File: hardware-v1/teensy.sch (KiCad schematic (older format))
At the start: 29 parts, among them J1 USB-MICRO-B-SHIELDED, P4 USB_POWER, P6 CORTEX_DEBUG, SW1 PROGRAM, U7 LP38691, U8 MK20DX256VLH7, U9 MKL02Z32VFG4, X1 CRYSTAL_SMD, Y2 32kHz

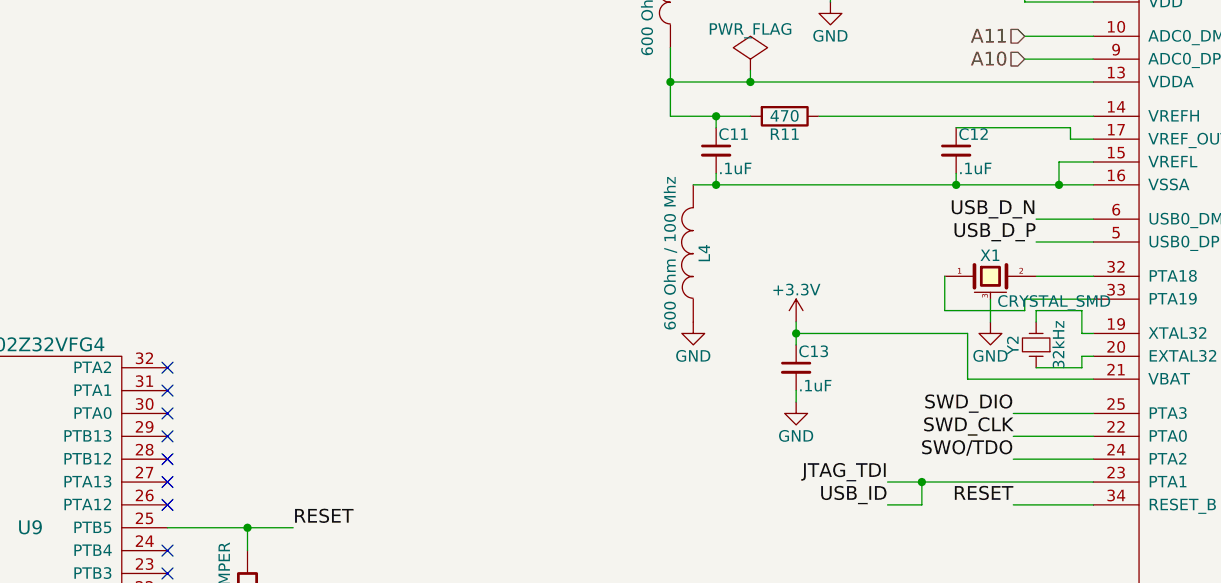
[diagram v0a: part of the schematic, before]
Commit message: Connect DEBUG line to MK02 reset line (with 0 ohm)
With a 0 ohm so that when PJRC comes up with bootloader that do not need
it, we will remove it.
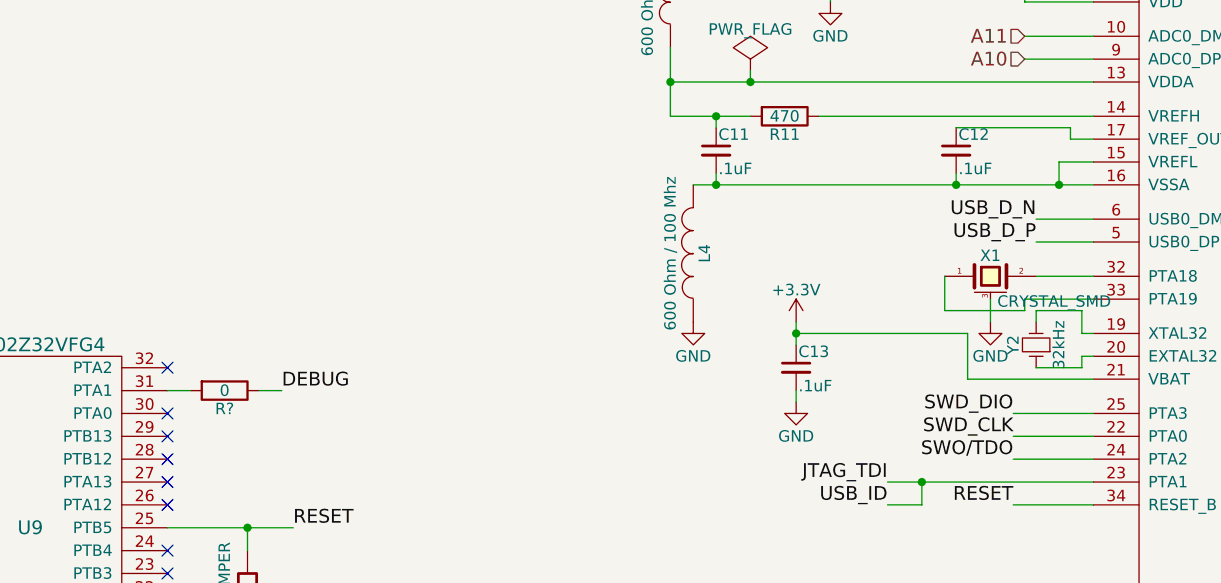
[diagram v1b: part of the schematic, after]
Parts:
- added R?: 0, symbol R
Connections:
- net DEBUG: now also R?.1
- net at U9.31 (PTA1): now also R?.2
- no-connect marks 21 -> 20
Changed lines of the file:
@@
 NoConn ~ 3000 3800
 NoConn ~ 3000 3700
-NoConn ~ 3000 3600
 NoConn ~ 3000 3500
 Text Label 1100 4200 2    60   ~ 0
@@
 	7050 2600 6900 2600
 Wire Wire Line
-	6900 2600 6900 2700
+	6900 2700 6900 2600
 Connection ~ 6900 2700
 Wire Wire Line
@@
 Wire Wire Line
 	4100 4900 4100 4950
+Wire Wire Line
+	3000 3600 3100 3600
+$Comp
+L R R?
+U 1 1 569DEDB1
+P 3250 3600
+F 0 "R?" V 3330 3600 50  0000 C CNN
+F 1 "0" V 3250 3600 50  0000 C CNN
+F 2 "" V 3180 3600 50  0000 C CNN
+F 3 "" H 3250 3600 50  0000 C CNN
+	1    3250 3600
+	0    1    1    0
+$EndComp
+Wire Wire Line
+	3400 3600 3500 3600
+Text Label 3500 3600 0    60   ~ 0
+DEBUG
 $EndSCHEMATC

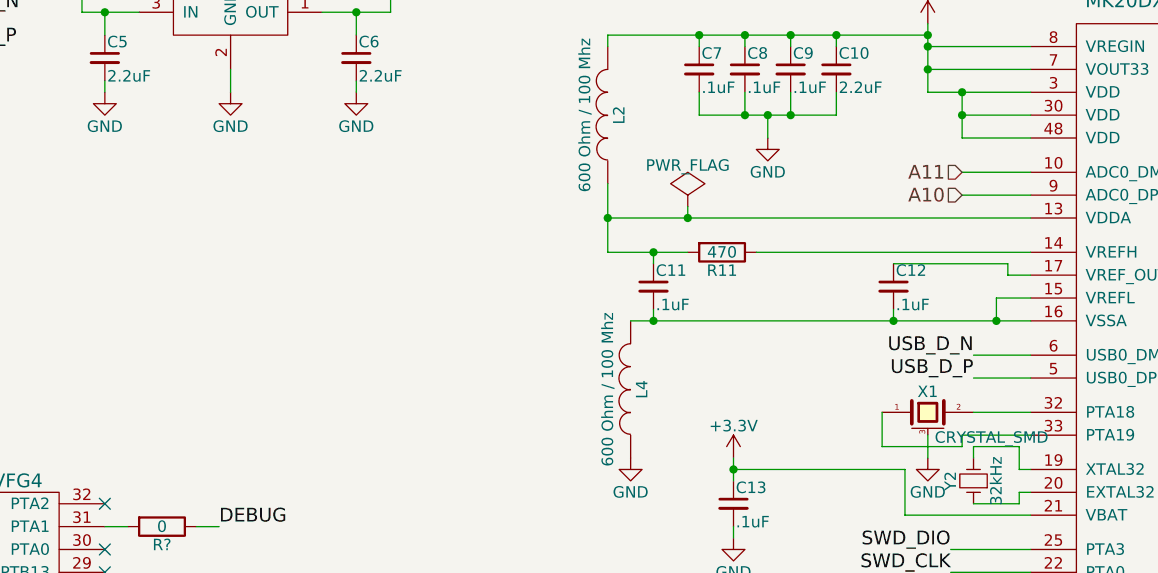
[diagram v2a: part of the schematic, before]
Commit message: Jumper to select Ser2 role + 3V voltage ref
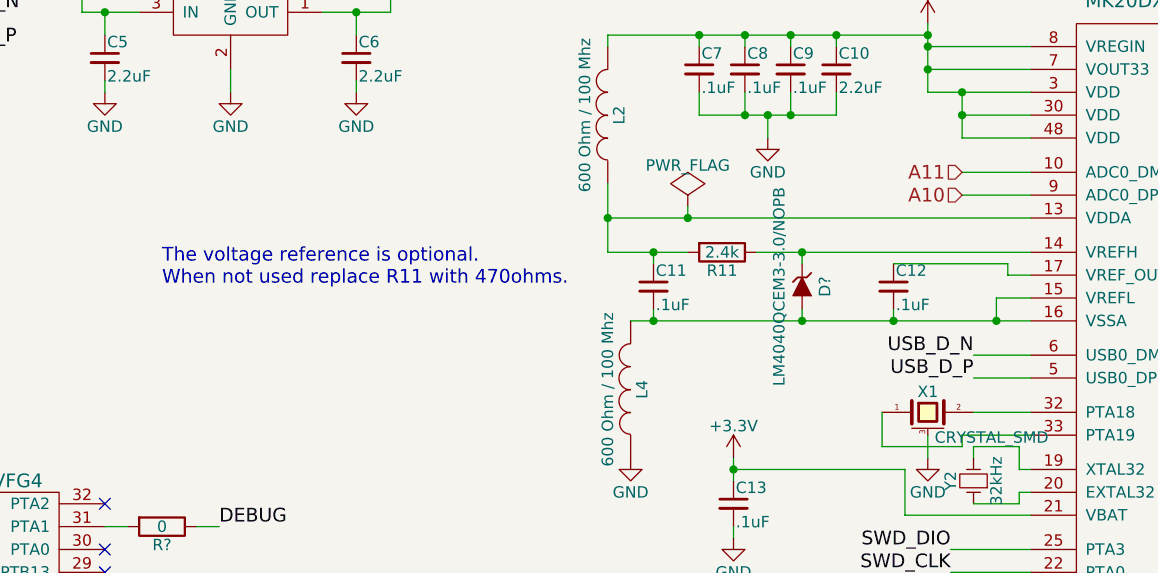
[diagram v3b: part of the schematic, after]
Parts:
- added D?: LM4040QCEM3-3.0/NOPB, symbol ZENERsmall
- R11: value 470 -> 2.4k
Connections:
- net at R11.1, U8.14 (VREFH): now also D?.1 (K)
- net at C11.2, C12.2, L4.2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: now also D?.2 (A)
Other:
- note added: "The voltage reference is optional.\nWhen not used replace R11 with 470ohms."
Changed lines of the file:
@@
 P 5700 2400
 F 0 "R11" V 5780 2400 50  0000 C CNN
-F 1 "470" V 5700 2400 50  0000 C CNN
+F 1 "2.4k" V 5700 2400 50  0000 C CNN
 F 2 "Resistors_SMD:R_0603_HandSoldering" V 5630 2400 30  0001 C CNN
 F 3 "" H 5700 2400 30  0000 C CNN
@@
 	7050 2600 6900 2600
 Wire Wire Line
-	6900 2700 6900 2600
+	6900 2600 6900 2700
 Connection ~ 6900 2700
 Wire Wire Line
@@
 Text Label 3500 3600 0    60   ~ 0
 DEBUG
+$Comp
+L ZENERsmall D?
+U 1 1 56ABEAB8
+P 6050 2550
+F 0 "D?" H 6050 2650 50  0000 C CNN
+F 1 "LM4040QCEM3-3.0/NOPB" H 6050 2450 50  0000 C CNN
+F 2 "" H 6050 2550 50  0000 C CNN
+F 3 "" H 6050 2550 50  0000 C CNN
+	1    6050 2550
+	0    1    1    0
+$EndComp
+Wire Wire Line
+	6050 2450 6050 2400
+Connection ~ 6050 2400
+Wire Wire Line
+	6050 2650 6050 2700
+Connection ~ 6050 2700
+Text Notes 3250 2550 0    60   ~ 0
+The voltage reference is optional.\nWhen not used replace R11 with 470ohms.
 $EndSCHEMATC

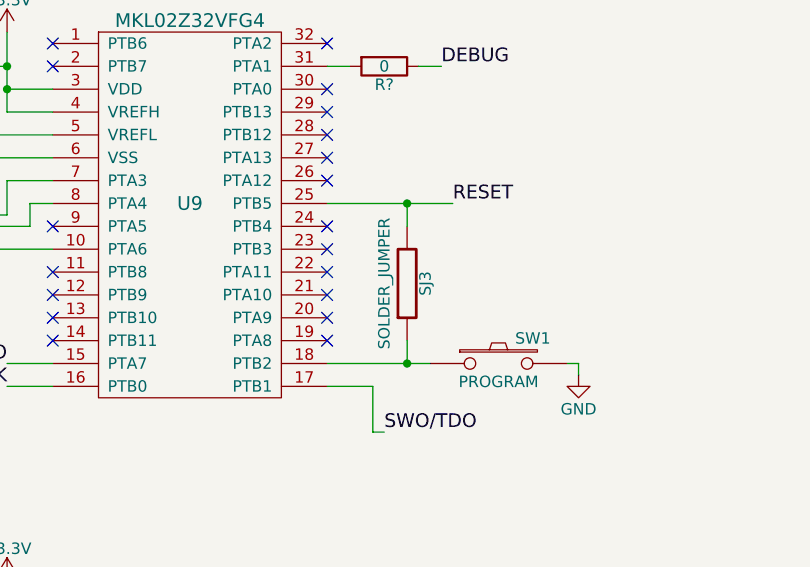
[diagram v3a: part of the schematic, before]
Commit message: Removed solder jumper on the reset line by a DNP 0 ohms
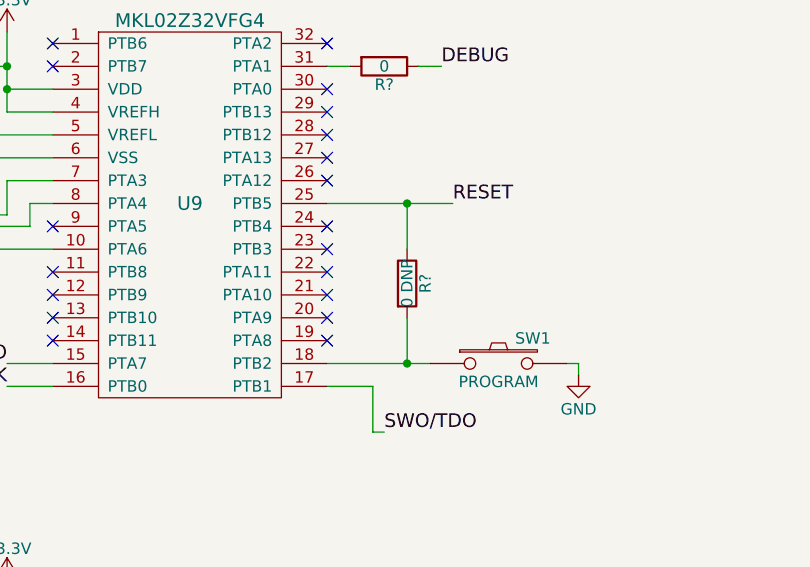
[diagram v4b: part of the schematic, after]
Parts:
- removed SJ3: SOLDER_JUMPER, bb:SolderJumper, symbol SOLDER_JUMPER
- added R?: 0 DNP, symbol R
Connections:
- net RESET: now also R?.1
- net at SW1.1, U9.18 (PTB2): now also R?.2
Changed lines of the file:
@@
 Wire Wire Line
 	1350 3600 1350 3650
-$Comp
-L SOLDER_JUMPER SJ3
-U 1 1 56652374
-P 3350 4550
-F 0 "SJ3" V 3430 4550 50  0000 C CNN
-F 1 "SOLDER_JUMPER" V 3250 4550 50  0000 C CNN
-F 2 "bb:SolderJumper" H 3350 4550 60  0001 C CNN
-F 3 "" H 3350 4550 60  0000 C CNN
-	1    3350 4550
-	1    0    0    1
-$EndComp
 Wire Wire Line
-	3350 4300 3350 4200
+	3350 4200 3350 4400
 Connection ~ 3350 4200
 Wire Wire Line
-	3350 4800 3350 4900
+	3350 4700 3350 4900
 Connection ~ 3350 4900
 Wire Wire Line
@@
 Text Notes 3250 2550 0    60   ~ 0
 The voltage reference is optional.\nWhen not used replace R11 with 470ohms.
+$Comp
+L R R?
+U 1 1 56AD8AD1
+P 3350 4550
+F 0 "R?" V 3430 4550 50  0000 C CNN
+F 1 "0 DNP" V 3350 4550 50  0000 C CNN
+F 2 "" V 3280 4550 50  0000 C CNN
+F 3 "" H 3350 4550 50  0000 C CNN
+	1    3350 4550
+	1    0    0    -1
+$EndComp
 $EndSCHEMATC

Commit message: re-annotate schematic
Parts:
- gave numbers to parts that had none: 3
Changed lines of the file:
@@
 $EndComp
 $Comp
-L GND #PWR033
+L GND #PWR44
 U 1 1 5658E841
 P 6850 5300
-F 0 "#PWR033" H 6850 5050 50  0001 C CNN
+F 0 "#PWR44" H 6850 5050 50  0001 C CNN
 F 1 "GND" H 6850 5150 50  0000 C CNN
 F 2 "" H 6850 5300 60  0000 C CNN
@@
 $EndComp
 $Comp
-L +3.3V #PWR034
+L +3.3V #PWR40
 U 1 1 5658ECFF
 P 1600 3450
-F 0 "#PWR034" H 1600 3300 50  0001 C CNN
+F 0 "#PWR40" H 1600 3300 50  0001 C CNN
 F 1 "+3.3V" H 1600 3590 50  0000 C CNN
 F 2 "" H 1600 3450 60  0000 C CNN
@@
 $EndComp
 $Comp
-L GND #PWR035
+L GND #PWR42
 U 1 1 5658ED8D
 P 1400 4050
-F 0 "#PWR035" H 1400 3800 50  0001 C CNN
+F 0 "#PWR42" H 1400 3800 50  0001 C CNN
 F 1 "GND" H 1400 3900 50  0000 C CNN
 F 2 "" H 1400 4050 60  0000 C CNN
@@
 $EndComp
 $Comp
-L GND #PWR036
+L GND #PWR43
 U 1 1 5658F088
 P 4100 4950
-F 0 "#PWR036" H 4100 4700 50  0001 C CNN
+F 0 "#PWR43" H 4100 4700 50  0001 C CNN
 F 1 "GND" H 4100 4800 50  0000 C CNN
 F 2 "" H 4100 4950 60  0000 C CNN
@@
 $EndComp
 $Comp
-L +3.3V #PWR037
+L +3.3V #PWR45
 U 1 1 56590BBB
 P 1600 5850
-F 0 "#PWR037" H 1600 5700 50  0001 C CNN
+F 0 "#PWR45" H 1600 5700 50  0001 C CNN
 F 1 "+3.3V" H 1600 5990 50  0000 C CNN
 F 2 "" H 1600 5850 60  0000 C CNN
@@
 NoConn ~ 1850 6300
 $Comp
-L GND #PWR038
+L GND #PWR35
 U 1 1 565927D7
 P 1700 2150
-F 0 "#PWR038" H 1700 1900 50  0001 C CNN
+F 0 "#PWR35" H 1700 1900 50  0001 C CNN
 F 1 "GND" H 1700 2000 50  0000 C CNN
 F 2 "" H 1700 2150 60  0000 C CNN
@@
 $EndComp
 $Comp
-L +3.3V #PWR039
+L +3.3V #PWR30
 U 1 1 56596469
 P 6600 1400
-F 0 "#PWR039" H 6600 1250 50  0001 C CNN
+F 0 "#PWR30" H 6600 1250 50  0001 C CNN
 F 1 "+3.3V" H 6600 1540 50  0000 C CNN
 F 2 "" H 6600 1400 60  0000 C CNN
@@
 $EndComp
 $Comp
-L GND #PWR040
+L GND #PWR34
 U 1 1 565968B4
 P 5900 1900
-F 0 "#PWR040" H 5900 1650 50  0001 C CNN
+F 0 "#PWR34" H 5900 1650 50  0001 C CNN
 F 1 "GND" H 5900 1750 50  0000 C CNN
 F 2 "" H 5900 1900 60  0000 C CNN
@@
 $EndComp
 $Comp
-L GND #PWR041
+L GND #PWR37
 U 1 1 56598327
 P 5300 3300
-F 0 "#PWR041" H 5300 3050 50  0001 C CNN
+F 0 "#PWR37" H 5300 3050 50  0001 C CNN
 F 1 "GND" H 5300 3150 50  0000 C CNN
 F 2 "" H 5300 3300 60  0000 C CNN
@@
 $EndComp
 $Comp
-L GND #PWR042
+L GND #PWR32
 U 1 1 565A6A4F
 P 3550 1700
-F 0 "#PWR042" H 3550 1450 50  0001 C CNN
+F 0 "#PWR32" H 3550 1450 50  0001 C CNN
 F 1 "GND" H 3550 1550 50  0000 C CNN
 F 2 "" H 3550 1700 60  0000 C CNN
@@
 $EndComp
 $Comp
-L +5V #PWR043
+L +5V #PWR28
 U 1 1 565A6A86
 P 2900 1250
-F 0 "#PWR043" H 2900 1100 50  0001 C CNN
+F 0 "#PWR28" H 2900 1100 50  0001 C CNN
 F 1 "+5V" H 2900 1390 50  0000 C CNN
 F 2 "" H 2900 1250 60  0000 C CNN
@@
 	3950 1350 4250 1350
 $Comp
-L +3.3V #PWR044
+L +3.3V #PWR29
 U 1 1 565A6D4A
 P 4250 1250
-F 0 "#PWR044" H 4250 1100 50  0001 C CNN
+F 0 "#PWR29" H 4250 1100 50  0001 C CNN
 F 1 "+3.3V" H 4250 1390 50  0000 C CNN
 F 2 "" H 4250 1250 60  0000 C CNN
@@
 	3550 1600 3550 1700
 $Comp
-L GND #PWR045
+L GND #PWR33
 U 1 1 565A70D1
 P 4100 1700
-F 0 "#PWR045" H 4100 1450 50  0001 C CNN
+F 0 "#PWR33" H 4100 1450 50  0001 C CNN
 F 1 "GND" H 4100 1550 50  0000 C CNN
 F 2 "" H 4100 1700 60  0000 C CNN
@@
 	3000 1650 3000 1700
 $Comp
-L GND #PWR046
+L GND #PWR31
 U 1 1 565AC891
 P 3000 1700
-F 0 "#PWR046" H 3000 1450 50  0001 C CNN
+F 0 "#PWR31" H 3000 1450 50  0001 C CNN
 F 1 "GND" H 3000 1550 50  0000 C CNN
 F 2 "" H 3000 1700 60  0000 C CNN
@@
 $EndComp
 $Comp
-L +5V #PWR047
+L +5V #PWR26
 U 1 1 565AEF07
 P 2300 750
-F 0 "#PWR047" H 2300 600 50  0001 C CNN
+F 0 "#PWR26" H 2300 600 50  0001 C CNN
 F 1 "+5V" H 2300 890 50  0000 C CNN
 F 2 "" H 2300 750 60  0000 C CNN
@@
 $EndComp
 $Comp
-L GND #PWR048
+L GND #PWR27
 U 1 1 565B08A1
 P 1500 1150
-F 0 "#PWR048" H 1500 900 50  0001 C CNN
+F 0 "#PWR27" H 1500 900 50  0001 C CNN
 F 1 "GND" H 1500 1000 50  0000 C CNN
 F 2 "" H 1500 1150 60  0000 C CNN
@@
 	8250 2450 8600 2450
 $Comp
-L GND #PWR049
+L GND #PWR36
 U 1 1 565BDF2E
 P 10200 2600
-F 0 "#PWR049" H 10200 2350 50  0001 C CNN
+F 0 "#PWR36" H 10200 2350 50  0001 C CNN
 F 1 "GND" H 10200 2450 50  0000 C CNN
 F 2 "" H 10200 2600 60  0000 C CNN
@@
 NoConn ~ 1800 4300
 $Comp
-L +3.3V #PWR050
+L +3.3V #PWR38
 U 1 1 567B1DAE
 P 5750 3300
-F 0 "#PWR050" H 5750 3150 50  0001 C CNN
+F 0 "#PWR38" H 5750 3150 50  0001 C CNN
 F 1 "+3.3V" H 5750 3440 50  0000 C CNN
 F 2 "" H 5750 3300 60  0000 C CNN
@@
 Connection ~ 5750 3350
 $Comp
-L GND #PWR051
+L GND #PWR41
 U 1 1 567B220D
 P 5750 3650
-F 0 "#PWR051" H 5750 3400 50  0001 C CNN
+F 0 "#PWR41" H 5750 3400 50  0001 C CNN
 F 1 "GND" H 5750 3500 50  0000 C CNN
 F 2 "" H 5750 3650 60  0000 C CNN
@@
 Connection ~ 5200 2250
 $Comp
-L PWR_FLAG #FLG052
+L PWR_FLAG #FLG2
 U 1 1 567B5BB9
 P 5550 2200
-F 0 "#FLG052" H 5550 2295 50  0001 C CNN
+F 0 "#FLG2" H 5550 2295 50  0001 C CNN
 F 1 "PWR_FLAG" H 5550 2380 50  0000 C CNN
 F 2 "" H 5550 2200 60  0000 C CNN
@@
 	6600 3200 6600 3300
 $Comp
-L GND #PWR053
+L GND #PWR39
 U 1 1 568579A5
 P 6600 3300
-F 0 "#PWR053" H 6600 3050 50  0001 C CNN
+F 0 "#PWR39" H 6600 3050 50  0001 C CNN
 F 1 "GND" H 6600 3150 50  0000 C CNN
 F 2 "" H 6600 3300 60  0000 C CNN
@@
 Connection ~ 1600 6150
 $Comp
-L GND #PWR054
+L GND #PWR46
 U 1 1 56858A76
 P 1100 6250
-F 0 "#PWR054" H 1100 6000 50  0001 C CNN
+F 0 "#PWR46" H 1100 6000 50  0001 C CNN
 F 1 "GND" H 1100 6100 50  0000 C CNN
 F 2 "" H 1100 6250 60  0000 C CNN
@@
 	3000 3600 3100 3600
 $Comp
-L R R?
+L R R3
 U 1 1 569DEDB1
 P 3250 3600
-F 0 "R?" V 3330 3600 50  0000 C CNN
+F 0 "R3" V 3330 3600 50  0000 C CNN
 F 1 "0" V 3250 3600 50  0000 C CNN
 F 2 "" V 3180 3600 50  0000 C CNN
@@
 DEBUG
 $Comp
-L ZENERsmall D?
+L ZENERsmall D7
 U 1 1 56ABEAB8
 P 6050 2550
-F 0 "D?" H 6050 2650 50  0000 C CNN
+F 0 "D7" H 6050 2650 50  0000 C CNN
 F 1 "LM4040QCEM3-3.0/NOPB" H 6050 2450 50  0000 C CNN
 F 2 "" H 6050 2550 50  0000 C CNN
@@
 The voltage reference is optional.\nWhen not used replace R11 with 470ohms.
 $Comp
-L R R?
+L R R13
 U 1 1 56AD8AD1
 P 3350 4550
-F 0 "R?" V 3430 4550 50  0000 C CNN
+F 0 "R13" V 3430 4550 50  0000 C CNN
 F 1 "0 DNP" V 3350 4550 50  0000 C CNN
 F 2 "" V 3280 4550 50  0000 C CNN
